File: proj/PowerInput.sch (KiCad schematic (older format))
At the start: 26 parts, among them Q1 MMBT3906, Q14 MMBT3904, Q2 IRLML6402, Q3 AOD417, U1 TL431AIDBZ, U2 LM393M

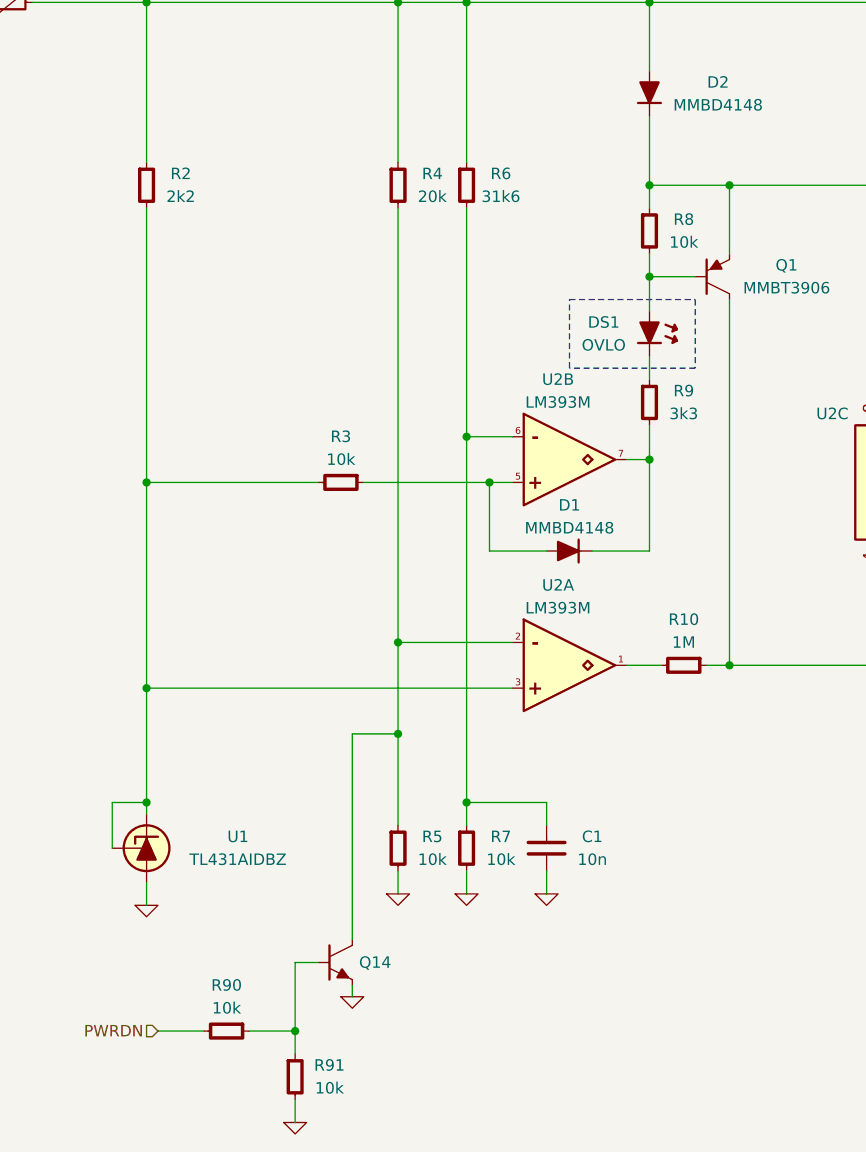
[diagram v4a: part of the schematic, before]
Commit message: Clean up resistor BOM
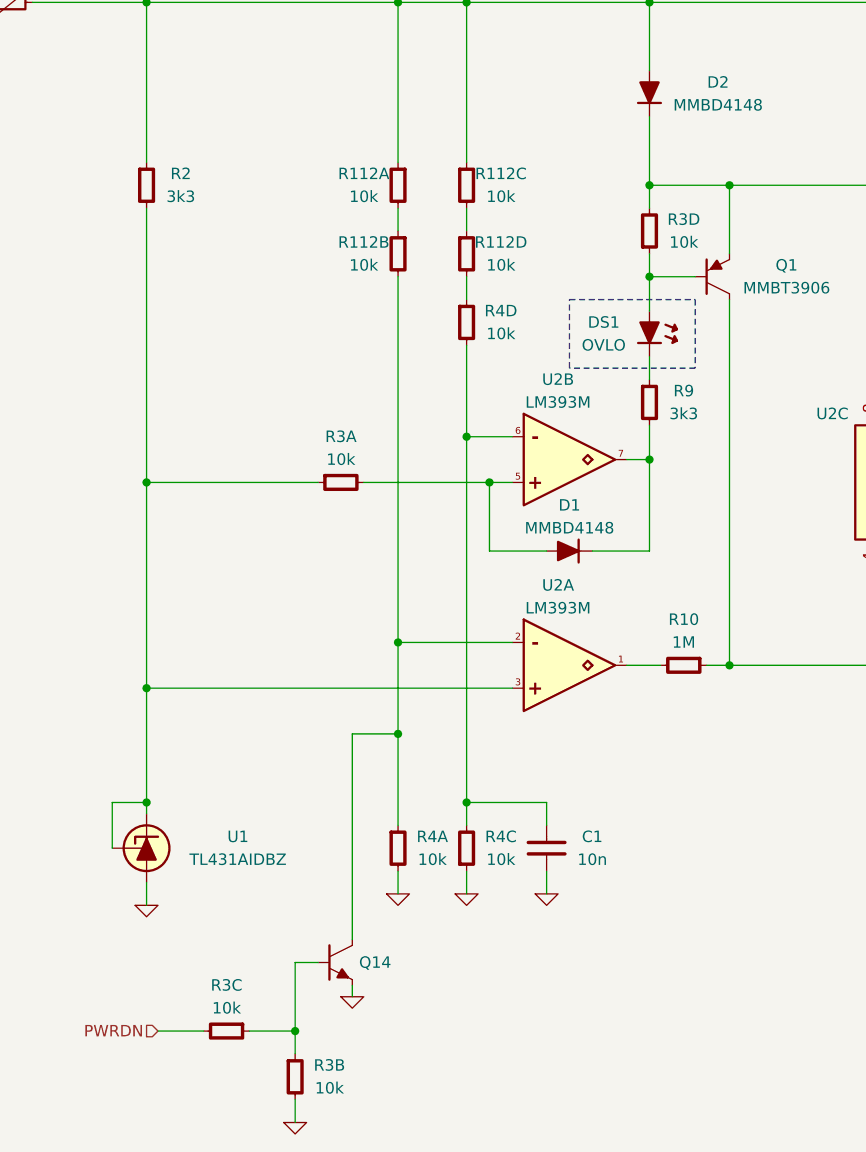
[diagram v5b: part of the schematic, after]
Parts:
- removed R3, R5, R7, R8, R90, R91: 10k, IPC7351-Nominal:RESC1005X40, symbol R-0402
- removed R4: 20k, IPC7351-Nominal:RESC1005X40, symbol R-0402
- removed R6: 31k6, IPC7351-Nominal:RESC1005X40, symbol R-0402
- added R112, R3, R4: 10k, IPC7351-Nominal:RESCAXE80P160X320X70-8, symbol RESPACK-4X0603-CONV
- R2: value 2k2 -> 3k3; BOM RES SMD 2k2 5% [0402] -> RES SMD 3.3k 5% [0402]
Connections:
- net GND: now also R3.7, R4.3, R4.8
- net PWRDN: now also R3.6
- net at D2.1, Q2.3, R1.2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: now also R112.1, R112.3
- net at D1.1, U2.5: now also R3.8
- net at C1.2, U2.6: now also R4.5, R4.6
- net at C2.1, D2.3, Q1.2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: now also R3.5
- net at DS1.2, Q1.1: now also R3.4
- net at Q14.3, U2.2: now also R112.7, R4.1
- net at R2.2, U1.1, U1.2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: now also R3.1
- net at Q14.1: now also R3.2, R3.3
- new net: R112.2, R112.8
- new net: R112.4, R112.6
- new net: R112.5, R4.4

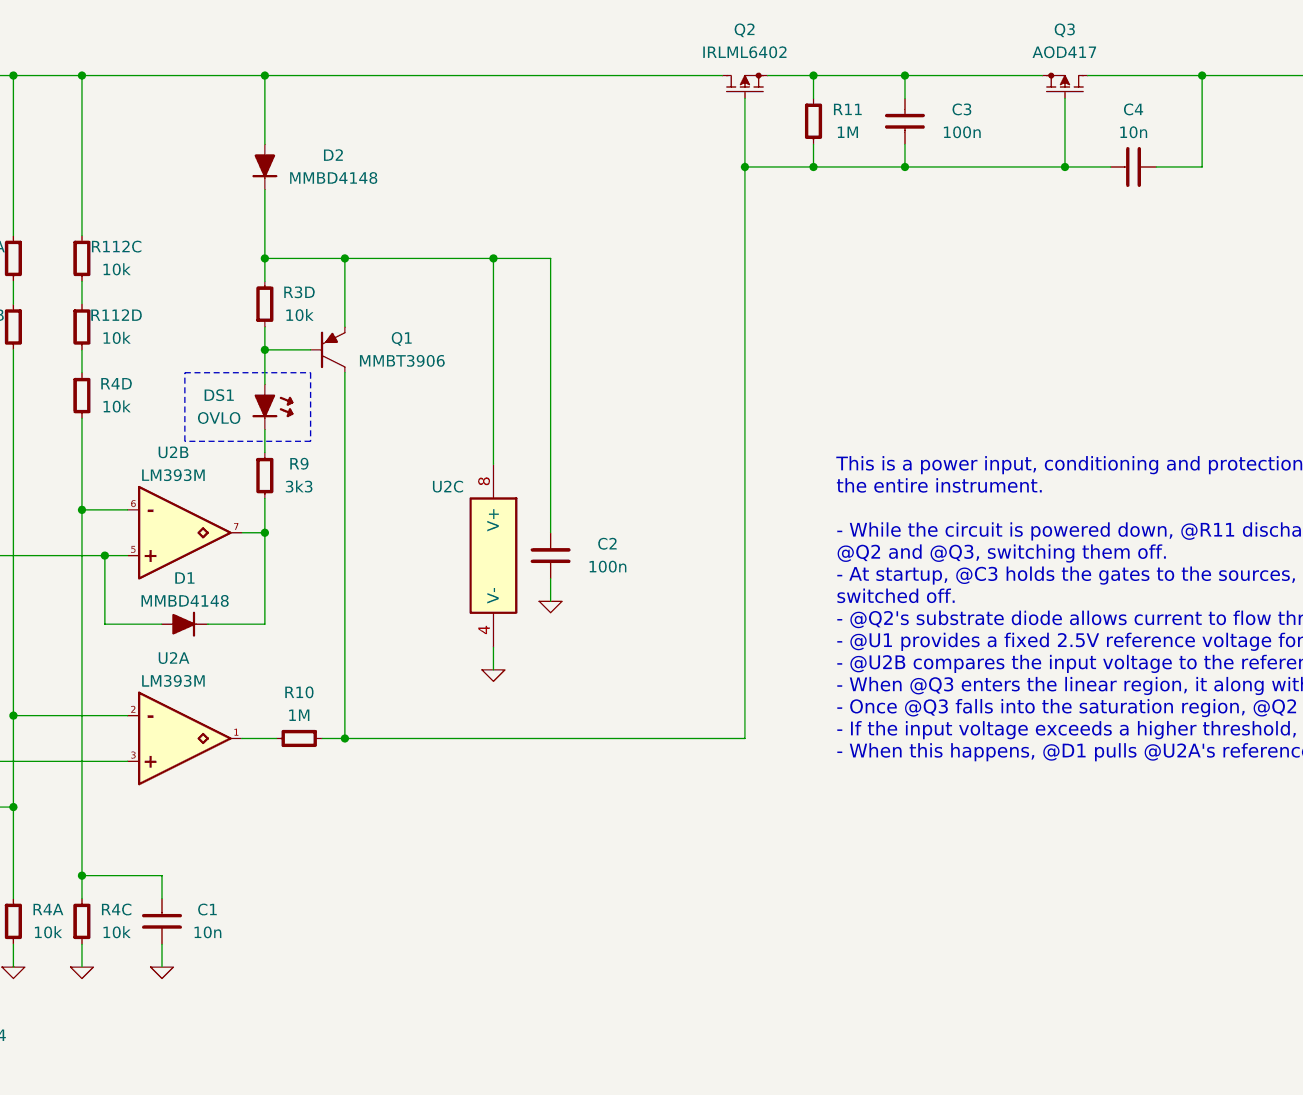
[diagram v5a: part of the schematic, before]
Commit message: Swap 0402 to 0603, add USB inrush protection
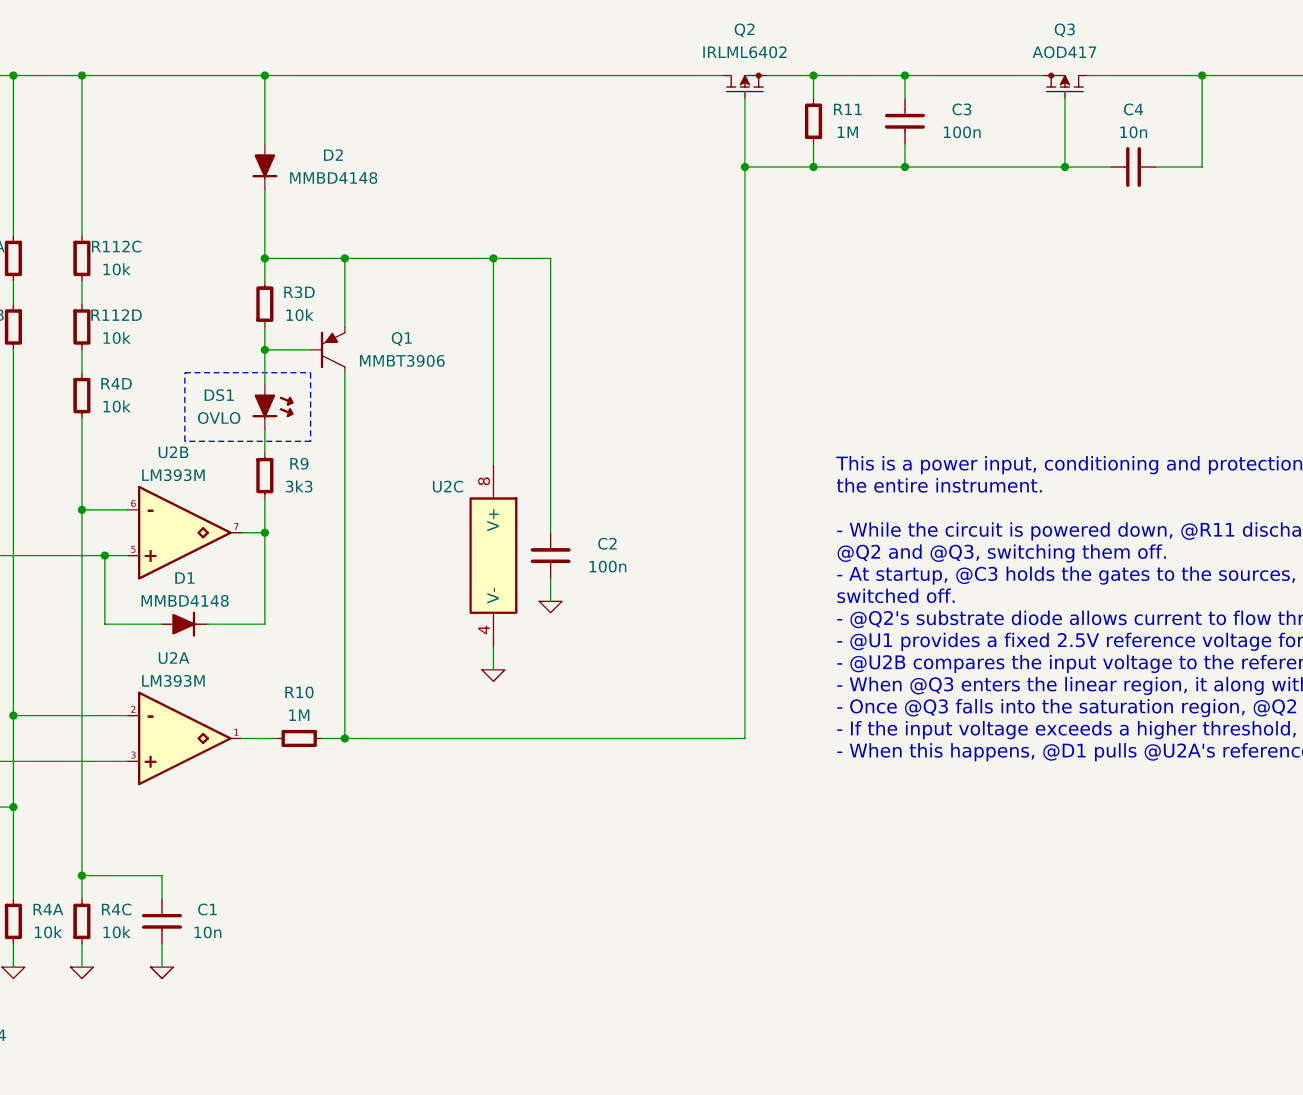
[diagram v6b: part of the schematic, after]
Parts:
- removed C1, C4: 10n, IPC7351-Nominal:CAPC1005X55, symbol C-0402
- removed R10, R11: 1M, IPC7351-Nominal:RESC1005X40, symbol R-0402
- removed R2, R9: 3k3, IPC7351-Nominal:RESC1005X40, symbol R-0402
- added C1, C4: 10n, IPC7351-Nominal:CAPC1608X55, symbol C-0603
- added R10, R11: 1M, IPC7351-Nominal:RESC1608X50, symbol R-0603
- added R2, R9: 3k3, IPC7351-Nominal:RESC1608X50, symbol R-0603
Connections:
- net GND: now also C1.2
- net OUT: now also C4.1
- net at D2.1, Q2.3, R1.2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: now also R2.1
- net at C3.1, Q2.2, Q3.2 (S): now also R11.2
- net at C3.2, Q1.3, Q2.1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: now also C4.2, R10.1, R11.1
- net at R4.5, R4.6, U2.6: now also C1.1
- net at D1.3, U2.7: now also R9.2
- net at DS1.1: now also R9.1
- net at U2.1: now also R10.2
- net at R3.1, U1.1, U1.2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: now also R2.2
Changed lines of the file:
@@
 Wire Wire Line
 	9900 2100 11100 2100
-$Comp
-L R-0402 R11
-U 1 1 54F4A395
-P 8700 2300
-F 0 "R11" H 8850 2350 50  0000 C CNN
-F 1 "1M" H 8850 2250 50  0000 C CNN
-F 2 "IPC7351-Nominal:RESC1005X40" H 8700 2300 50  0001 C CNN
-F 3 "" H 8700 2350 60  0000 C CNN
-F 4 "Value" H 8700 2300 60  0001 C CNN "Manuf"
-F 5 "RES SMD 1M 5% [0402]" H 9450 2850 60  0001 C CNN "BOM"
-	1    8700 2300
-	1    0    0    -1
-$EndComp
 Wire Wire Line
 	8700 2400 8700 2500
@@
 	9100 2400 9100 2500
 Connection ~ 9100 2500
-$Comp
-L C-0402 C4
-U 1 1 54F4AFC5
-P 10100 2500
-F 0 "C4" V 10350 2500 50  0000 C CNN
-F 1 "10n" V 10250 2500 50  0000 C CNN
-F 2 "IPC7351-Nominal:CAPC1005X55" H 10100 2500 50  0001 C CNN
-F 3 "" H 10090 2475 60  0000 C CNN
-F 4 "Value" H 10100 2500 60  0001 C CNN "Manuf"
-F 5 "CAP MLCC 10n ≥X5R 25V 10% [0402]" H 10900 3050 60  0001 C CNN "BOM"
-	1    10100 2500
-	0    1    -1   0
-$EndComp
 Connection ~ 9800 2500
 Wire Wire Line
@@
 F 3 "" V 5900 4250 60  0000 C CNN
 	2    5900 4100
-	1    0    0    -1
-$EndComp
-$Comp
-L R-0402 R9
-U 1 1 54F4B82A
-P 6300 3850
-F 0 "R9" H 6450 3900 50  0000 C CNN
-F 1 "3k3" H 6450 3800 50  0000 C CNN
-F 2 "IPC7351-Nominal:RESC1005X40" H 6300 3850 50  0001 C CNN
-F 3 "" H 6300 3900 60  0000 C CNN
-F 4 "Value" H 6300 3850 60  0001 C CNN "Manuf"
-F 5 "RES SMD 3.3k 5% [0402]" H 7050 4400 60  0001 C CNN "BOM"
-	1    6300 3850
 	1    0    0    -1
 $EndComp
@@
 	1    0    0    -1
 $EndComp
-$Comp
-L R-0402 R10
-U 1 1 54F4BAEB
-P 6450 5000
-F 0 "R10" V 6250 5000 50  0000 C CNN
-F 1 "1M" V 6350 5000 50  0000 C CNN
-F 2 "IPC7351-Nominal:RESC1005X40" H 6450 5000 50  0001 C CNN
-F 3 "" H 6450 5050 60  0000 C CNN
-F 4 "Value" H 6450 5000 60  0001 C CNN "Manuf"
-F 5 "RES SMD 1M 5% [0402]" H 7200 5550 60  0001 C CNN "BOM"
-	1    6450 5000
-	0    1    1    0
-$EndComp
 Wire Wire Line
 	6350 5000 6200 5000
@@
 Connection ~ 4100 5100
 $Comp
-L GND #PWR0198
+L GND #PWR0191
 U 1 1 54F4C586
 P 4100 6050
-F 0 "#PWR0198" H 4100 6050 30  0001 C CNN
+F 0 "#PWR0191" H 4100 6050 30  0001 C CNN
 F 1 "GND" H 4100 5980 30  0001 C CNN
 F 2 "" H 4100 6050 60  0000 C CNN
@@
 $EndComp
 $Comp
-L GND #PWR0199
+L GND #PWR0192
 U 1 1 54F4C600
 P 5200 6000
-F 0 "#PWR0199" H 5200 6000 30  0001 C CNN
+F 0 "#PWR0192" H 5200 6000 30  0001 C CNN
 F 1 "GND" H 5200 5930 30  0001 C CNN
 F 2 "" H 5200 6000 60  0000 C CNN
@@
 	5200 6000 5200 5900
 $Comp
-L GND #PWR0200
+L GND #PWR0193
 U 1 1 54F4C674
 P 5500 6000
-F 0 "#PWR0200" H 5500 6000 30  0001 C CNN
+F 0 "#PWR0193" H 5500 6000 30  0001 C CNN
 F 1 "GND" H 5500 5930 30  0001 C CNN
 F 2 "" H 5500 6000 60  0000 C CNN
@@
 	3950 5600 4100 5600
 Connection ~ 4100 5600
-$Comp
-L R-0402 R2
-U 1 1 54F4CB69
-P 4100 2900
-F 0 "R2" H 4250 2950 50  0000 C CNN
-F 1 "3k3" H 4250 2850 50  0000 C CNN
-F 2 "IPC7351-Nominal:RESC1005X40" H 4100 2900 50  0001 C CNN
-F 3 "" H 4100 2950 60  0000 C CNN
-F 4 "Value" H 4100 2900 60  0001 C CNN "Manuf"
-F 5 "RES SMD 3.3k 5% [0402]" H 4850 3450 60  0001 C CNN "BOM"
-	1    4100 2900
-	1    0    0    -1
-$EndComp
 Connection ~ 4100 4200
 Wire Wire Line
@@
 Connection ~ 7300 2900
 $Comp
-L GND #PWR0201
+L GND #PWR0194
 U 1 1 54F4D4FF
 P 7550 4400
-F 0 "#PWR0201" H 7550 4400 30  0001 C CNN
+F 0 "#PWR0194" H 7550 4400 30  0001 C CNN
 F 1 "GND" H 7550 4330 30  0001 C CNN
 F 2 "" H 7550 4400 60  0000 C CNN
@@
 	7550 4400 7550 4300
 $Comp
-L GND #PWR0202
+L GND #PWR0195
 U 1 1 54F4D5D3
 P 7300 4700
-F 0 "#PWR0202" H 7300 4700 30  0001 C CNN
+F 0 "#PWR0195" H 7300 4700 30  0001 C CNN
 F 1 "GND" H 7300 4630 30  0001 C CNN
 F 2 "" H 7300 4700 60  0000 C CNN
@@
 Wire Wire Line
 	7300 4700 7300 4600
-$Comp
-L C-0402 C1
-U 1 1 54F4E7EE
-P 5850 5800
-F 0 "C1" H 6050 5750 50  0000 C CNN
-F 1 "10n" H 6050 5850 50  0000 C CNN
-F 2 "IPC7351-Nominal:CAPC1005X55" H 5850 5800 50  0001 C CNN
-F 3 "" H 5840 5775 60  0000 C CNN
-F 4 "Value" H 5850 5800 60  0001 C CNN "Manuf"
-F 5 "CAP MLCC 10n ≥X5R 25V 10% [0402]" H 6650 6350 60  0001 C CNN "BOM"
-	1    5850 5800
-	1    0    0    1
-$EndComp
 Wire Wire Line
 	5850 5700 5850 5600
@@
 Connection ~ 5500 5600
 $Comp
-L GND #PWR0203
+L GND #PWR0196
 U 1 1 54F4E909
 P 5850 6000
-F 0 "#PWR0203" H 5850 6000 30  0001 C CNN
+F 0 "#PWR0196" H 5850 6000 30  0001 C CNN
 F 1 "GND" H 5850 5930 30  0001 C CNN
 F 2 "" H 5850 6000 60  0000 C CNN
@@
 	5000 5300 5000 6200
 $Comp
-L GND #PWR0204
+L GND #PWR0197
 U 1 1 54F7D2C2
 P 5000 6450
-F 0 "#PWR0204" H 5000 6450 30  0001 C CNN
+F 0 "#PWR0197" H 5000 6450 30  0001 C CNN
 F 1 "GND" H 5000 6380 30  0001 C CNN
 F 2 "" H 5000 6450 60  0000 C CNN
@@
 	4750 6300 4850 6300
 $Comp
-L GND #PWR0205
+L GND #PWR0198
 U 1 1 54F7D63A
 P 4750 7000
-F 0 "#PWR0205" H 4750 7000 30  0001 C CNN
+F 0 "#PWR0198" H 4750 7000 30  0001 C CNN
 F 1 "GND" H 4750 6930 30  0001 C CNN
 F 2 "" H 4750 7000 60  0000 C CNN
@@
 	1    0    0    1
 $EndComp
+$Comp
+L C-0603 C4
+U 1 1 54FFC16C
+P 10100 2500
+F 0 "C4" V 9850 2500 50  0000 C CNN
+F 1 "10n" V 9950 2500 50  0000 C CNN
+F 2 "IPC7351-Nominal:CAPC1608X55" H 10100 2500 50  0001 C CNN
+F 3 "" H 10090 2475 60  0000 C CNN
+F 4 "Value" H 10100 2500 60  0001 C CNN "Manuf"
+F 5 "CAP MLCC 10n ≥X5R 50V 10% [0603]" H 10900 3050 60  0001 C CNN "BOM"
+	1    10100 2500
+	0    1    1    0
+$EndComp
+$Comp
+L C-0603 C1
+U 1 1 54FFDFEA
+P 5850 5800
+F 0 "C1" H 6050 5850 50  0000 C CNN
+F 1 "10n" H 6050 5750 50  0000 C CNN
+F 2 "IPC7351-Nominal:CAPC1608X55" H 5850 5800 50  0001 C CNN
+F 3 "" H 5840 5775 60  0000 C CNN
+F 4 "Value" H 5850 5800 60  0001 C CNN "Manuf"
+F 5 "CAP MLCC 10n ≥X5R 50V 10% [0603]" H 6650 6350 60  0001 C CNN "BOM"
+	1    5850 5800
+	1    0    0    -1
+$EndComp
+$Comp
+L R-0603 R2
+U 1 1 54FF9E0A
+P 4100 2900
+F 0 "R2" H 4250 2950 50  0000 C CNN
+F 1 "3k3" H 4250 2850 50  0000 C CNN
+F 2 "IPC7351-Nominal:RESC1608X50" H 4100 2900 50  0001 C CNN
+F 3 "" H 4100 2950 60  0000 C CNN
+F 4 "Value" H 4100 2900 60  0001 C CNN "Manuf"
+F 5 "RES SMD 3.3k 5% [0603]" H 4850 3450 60  0001 C CNN "BOM"
+	1    4100 2900
+	1    0    0    -1
+$EndComp
+$Comp
+L R-0603 R10
+U 1 1 54FFB7A7
+P 6450 5000
+F 0 "R10" V 6250 5000 50  0000 C CNN
+F 1 "1M" V 6350 5000 50  0000 C CNN
+F 2 "IPC7351-Nominal:RESC1608X50" H 6450 5000 50  0001 C CNN
+F 3 "" H 6450 5050 60  0000 C CNN
+F 4 "Value" H 6450 5000 60  0001 C CNN "Manuf"
+F 5 "RES SMD 1M 5% [0603]" H 7200 5550 60  0001 C CNN "BOM"
+	1    6450 5000
+	0    1    1    0
+$EndComp
+$Comp
+L R-0603 R9
+U 1 1 54FFBA26
+P 6300 3850
+F 0 "R9" H 6450 3900 50  0000 C CNN
+F 1 "3k3" H 6450 3800 50  0000 C CNN
+F 2 "IPC7351-Nominal:RESC1608X50" H 6300 3850 50  0001 C CNN
+F 3 "" H 6300 3900 60  0000 C CNN
+F 4 "Value" H 6300 3850 60  0001 C CNN "Manuf"
+F 5 "RES SMD 3.3k 5% [0603]" H 7050 4400 60  0001 C CNN "BOM"
+	1    6300 3850
+	1    0    0    -1
+$EndComp
+$Comp
+L R-0603 R11
+U 1 1 54FFD783
+P 8700 2300
+F 0 "R11" H 8550 2250 50  0000 C CNN
+F 1 "1M" H 8550 2350 50  0000 C CNN
+F 2 "IPC7351-Nominal:RESC1608X50" H 8700 2300 50  0001 C CNN
+F 3 "" H 8700 2350 60  0000 C CNN
+F 4 "Value" H 8700 2300 60  0001 C CNN "Manuf"
+F 5 "RES SMD 1M 5% [0603]" H 9450 2850 60  0001 C CNN "BOM"
+	1    8700 2300
+	-1   0    0    1
+$EndComp
 $EndSCHEMATC
